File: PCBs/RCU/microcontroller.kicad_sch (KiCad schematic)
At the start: 23 parts, among them J200 USB_C_Receptacle_USB2.0, J201 Conn_01x05, SW201 SW_Push, U200 STM32G0B1CBT6, Y200 16MHz

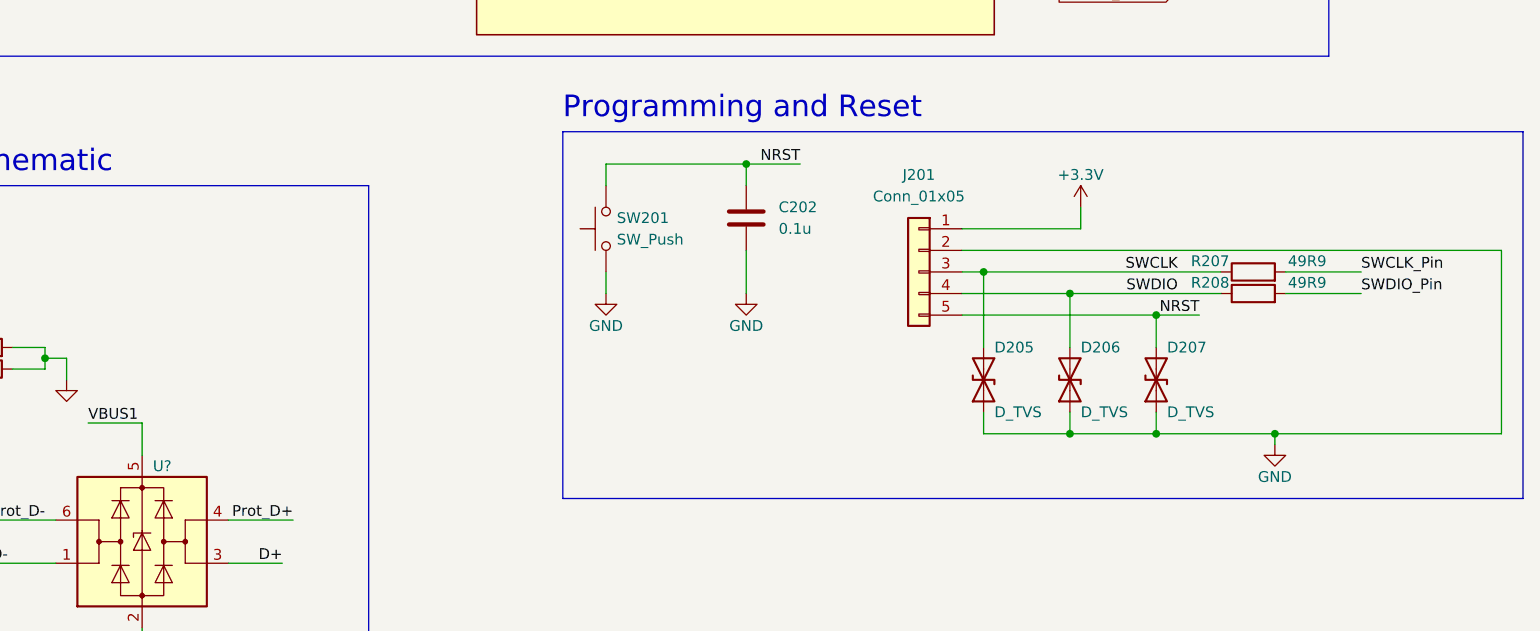
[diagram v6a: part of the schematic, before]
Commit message: Added ESD protection to 3.3V pin of SWD connector, and made motor sheet larger
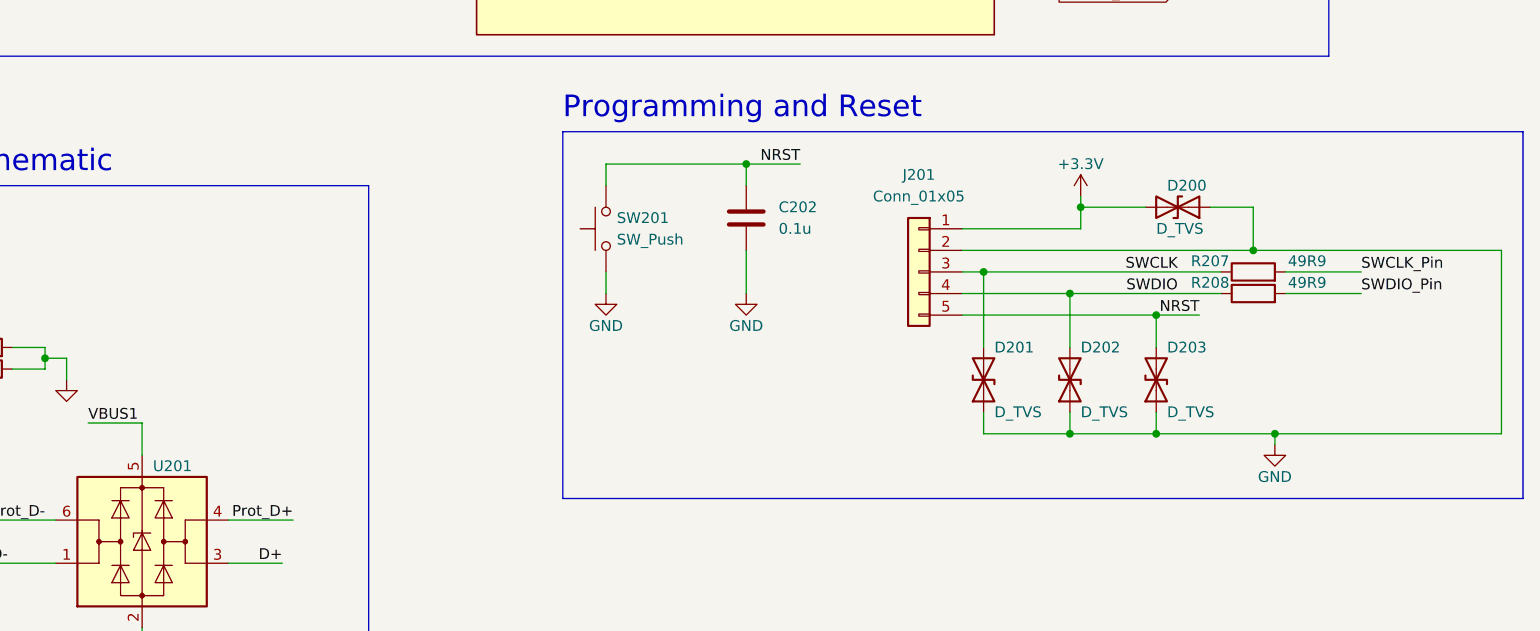
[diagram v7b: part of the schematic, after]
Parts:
- added D200: D_TVS, symbol Device:D_TVS
- gave numbers to parts that had none: 1
- renumbered D205 to D201, D206 to D202, D207 to D203
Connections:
- net +3V3: now also D200.2 (A2)
- net GND: now also D200.1 (A1)
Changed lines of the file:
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@@
   (junction (at 93.98 147.32) (diameter 0) (color 0 0 0 0)
   )
+  (junction (at 215.9 129.54) (diameter 0) (color 0 0 0 0)
+  )
   (junction (at 214.63 139.7) (diameter 0) (color 0 0 0 0)
+  )
+  (junction (at 236.22 134.62) (diameter 0) (color 0 0 0 0)
   )
   (junction (at 224.79 142.24) (diameter 0) (color 0 0 0 0)
@@
   (no_connect (at 213.36 99.06))
   (no_connect (at 76.2 171.45))
+  (wire (pts (xy 236.22 129.54) (xy 236.22 134.62))
+    (stroke (width 0) (type default) (color 0 0 0 0))
+  )
   (wire (pts (xy 76.2 140.97) (xy 81.28 140.97))
     (stroke (width 0) (type default) (color 0 0 0 0))
@@
     (stroke (width 0) (type default) (color 0 0 0 0))
   )
+  (wire (pts (xy 231.14 129.54) (xy 236.22 129.54))
+    (stroke (width 0) (type default) (color 0 0 0 0))
+  )
   (wire (pts (xy 64.77 73.66) (xy 77.47 73.66))
     (stroke (width 0) (type default) (color 0 0 0 0))
@@
     (stroke (width 0) (type default) (color 0 0 0 0))
   )
+  (wire (pts (xy 215.9 129.54) (xy 223.52 129.54))
+    (stroke (width 0) (type default) (color 0 0 0 0))
+  )
   (wire (pts (xy 93.98 147.32) (xy 96.52 147.32))
     (stroke (width 0) (type default) (color 0 0 0 0))
@@
     (stroke (width 0) (type default) (color 0 0 0 0))
   )
-  (wire (pts (xy 201.93 134.62) (xy 265.43 134.62))
+  (wire (pts (xy 201.93 134.62) (xy 236.22 134.62))
     (stroke (width 0) (type default) (color 0 0 0 0))
   )
@@
     (stroke (width 0) (type default) (color 0 0 0 0))
   )
+  (wire (pts (xy 215.9 129.54) (xy 215.9 128.27))
+    (stroke (width 0) (type default) (color 0 0 0 0))
+  )
   (wire (pts (xy 90.17 146.05) (xy 93.98 146.05))
     (stroke (width 0) (type default) (color 0 0 0 0))
@@
   )
   (wire (pts (xy 87.63 73.66) (xy 88.9 73.66))
+    (stroke (width 0) (type default) (color 0 0 0 0))
+  )
+  (wire (pts (xy 236.22 134.62) (xy 265.43 134.62))
     (stroke (width 0) (type default) (color 0 0 0 0))
   )
@@
   (symbol (lib_id "Device:D_TVS") (at 224.79 149.86 90) (unit 1)
     (in_bom yes) (on_board yes)
-    (property "Reference" "D207" (id 0) (at 226.06 146.05 90)
+    (property "Reference" "D203" (id 0) (at 226.06 146.05 90)
       (effects (font (size 1.27 1.27)) (justify right))
     )
@@
   (symbol (lib_id "Device:D_TVS") (at 204.47 149.86 90) (unit 1)
     (in_bom yes) (on_board yes)
-    (property "Reference" "D205" (id 0) (at 205.74 146.05 90)
+    (property "Reference" "D201" (id 0) (at 205.74 146.05 90)
       (effects (font (size 1.27 1.27)) (justify right))
     )
@@
     (pin "2")
   )
-  (symbol (lib_id "power:+3.3V") (at 215.9 129.54 0) (unit 1)
-    (in_bom yes) (on_board yes)
-    (property "Reference" "#PWR?" (id 0) (at 215.9 133.35 0)
-      (effects (font (size 1.27 1.27)) hide)
-    )
-    (property "Value" "+3.3V" (id 1) (at 215.9 125.73 0))
-    (property "Footprint" "" (id 2) (at 215.9 129.54 0)
-      (effects (font (size 1.27 1.27)) hide)
-    )
-    (property "Datasheet" "" (id 3) (at 215.9 129.54 0)
+  (symbol (lib_id "power:+3.3V") (at 215.9 128.27 0) (unit 1)
+    (in_bom yes) (on_board yes)
+    (property "Reference" "#PWR?" (id 0) (at 215.9 132.08 0)
+      (effects (font (size 1.27 1.27)) hide)
+    )
+    (property "Value" "+3.3V" (id 1) (at 215.9 124.46 0))
+    (property "Footprint" "" (id 2) (at 215.9 128.27 0)
+      (effects (font (size 1.27 1.27)) hide)
+    )
+    (property "Datasheet" "" (id 3) (at 215.9 128.27 0)
       (effects (font (size 1.27 1.27)) hide)
     )
@@
   (symbol (lib_id "Device:D_TVS") (at 214.63 149.86 90) (unit 1)
     (in_bom yes) (on_board yes)
-    (property "Reference" "D206" (id 0) (at 215.9 146.05 90)
+    (property "Reference" "D202" (id 0) (at 215.9 146.05 90)
       (effects (font (size 1.27 1.27)) (justify right))
     )
@@
   (symbol (lib_id "Power_Protection:USBLC6-2SC6") (at 105.41 168.91 0) (unit 1)
     (in_bom yes) (on_board yes)
-    (property "Reference" "U?" (id 0) (at 106.68 160.02 0)
+    (property "Reference" "U201" (id 0) (at 106.68 160.02 0)
       (effects (font (size 1.27 1.27)) (justify left))
     )
@@
     (pin "1")
   )
+  (symbol (lib_id "Device:D_TVS") (at 227.33 129.54 180) (unit 1)
+    (in_bom yes) (on_board yes)
+    (property "Reference" "D200" (id 0) (at 226.06 127 0)
+      (effects (font (size 1.27 1.27)) (justify right))
+    )
+    (property "Value" "D_TVS" (id 1) (at 224.79 132.08 0)
+      (effects (font (size 1.27 1.27)) (justify right))
+    )
+    (property "Footprint" "" (id 2) (at 227.33 129.54 0)
+      (effects (font (size 1.27 1.27)) hide)
+    )
+    (property "Datasheet" "~" (id 3) (at 227.33 129.54 0)
+      (effects (font (size 1.27 1.27)) hide)
+    )
+    (pin "1")
+    (pin "2")
+  )
   (symbol (lib_id "power:+3.3V") (at 97.79 49.53 0) (unit 1)

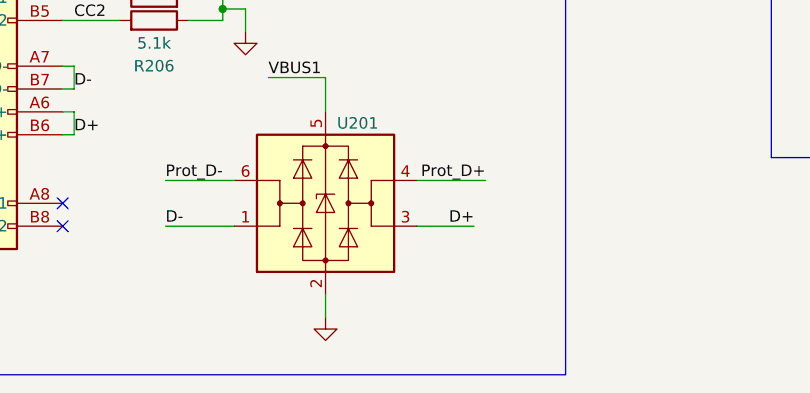
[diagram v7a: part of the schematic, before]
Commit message: Corrected resistor values for stepping down encoder output voltage
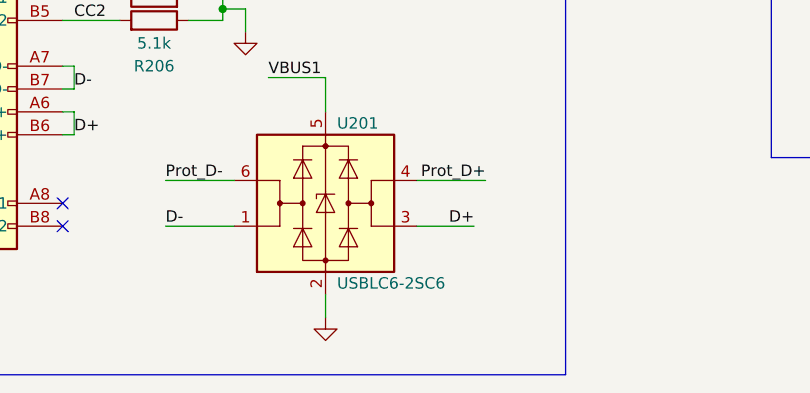
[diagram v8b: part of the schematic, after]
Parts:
- U201: value (none) -> USBLC6-2SC6; footprint (none) -> Package_TO_SOT_SMD:SOT-23-6
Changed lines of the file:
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@@
       (effects (font (size 1.27 1.27)) (justify left))
     )
-    (property "Value" "" (id 1) (at 106.68 177.8 0)
+    (property "Value" "USBLC6-2SC6" (id 1) (at 106.68 177.8 0)
       (effects (font (size 1.27 1.27)) (justify left))
     )
-    (property "Footprint" "" (id 2) (at 105.41 181.61 0)
+    (property "Footprint" "Package_TO_SOT_SMD:SOT-23-6" (id 2) (at 105.41 181.61 0)
       (effects (font (size 1.27 1.27)) hide)
     )
